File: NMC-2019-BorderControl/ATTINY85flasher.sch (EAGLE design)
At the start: 13 parts, among them J1 ICSP-LO-SILK

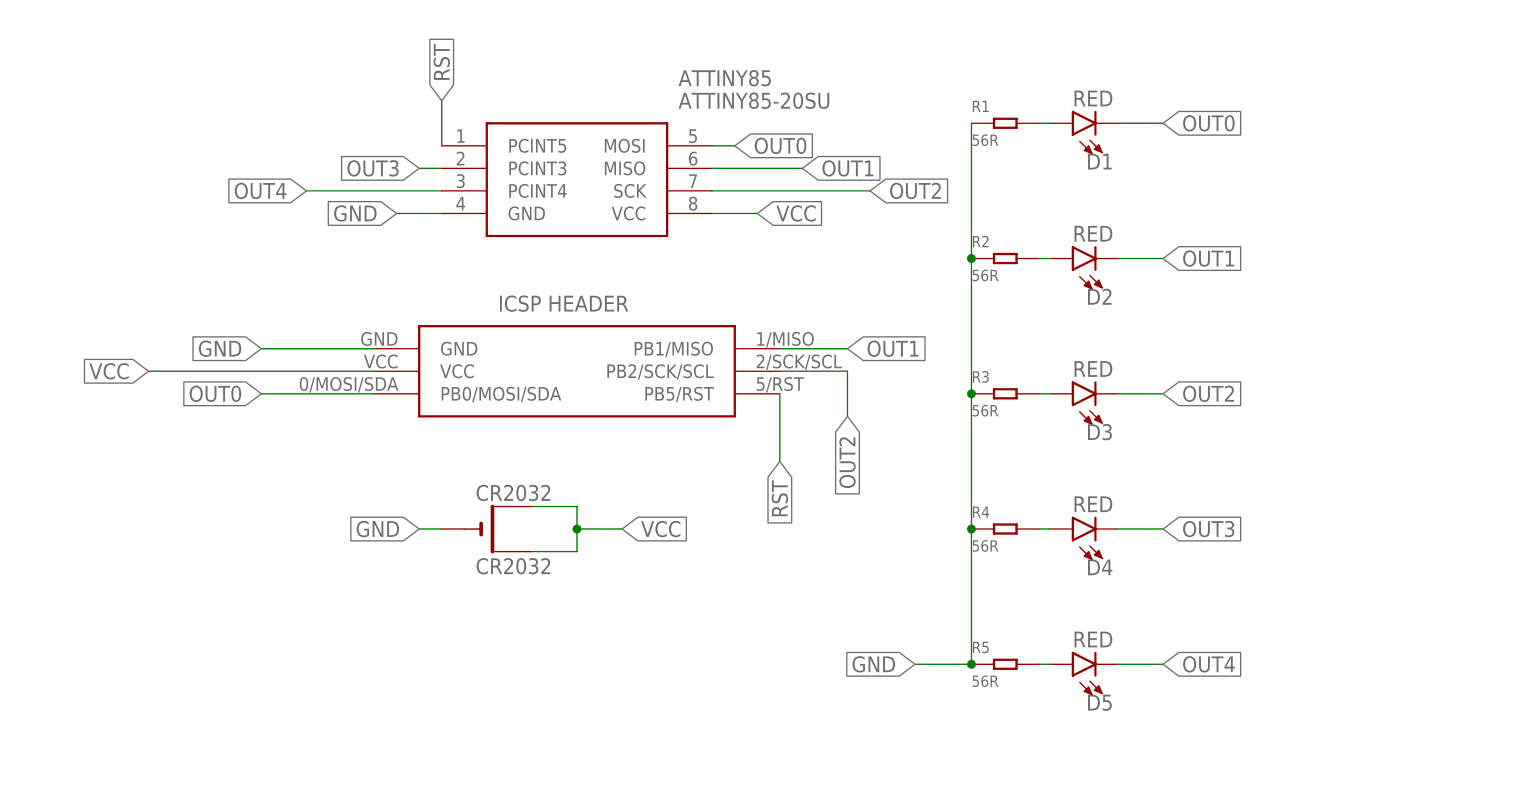
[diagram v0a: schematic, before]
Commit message: corrected polarity
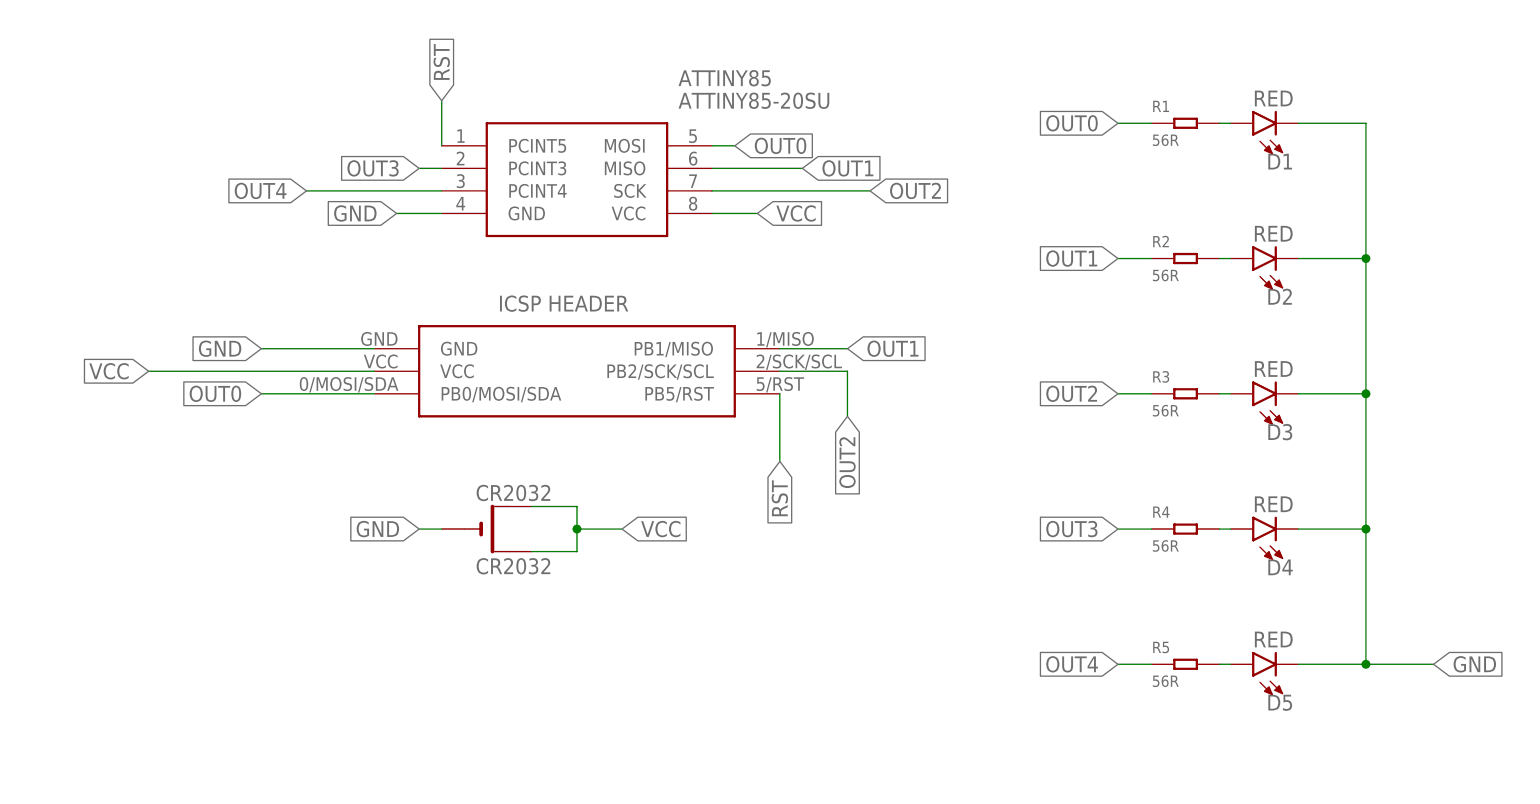
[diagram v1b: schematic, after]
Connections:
- net GND: now also D1.C, D2.C, D3.C, D4.C, D5.C; no longer R1.1, R2.1, R3.1, R4.1, R5.1
- net OUT0: now also R1.1; no longer D1.C
- net OUT1: now also R2.1; no longer D2.C
- net OUT2: now also R3.1; no longer D3.C
- net OUT3: now also R4.1; no longer D4.C
- net OUT4: now also R5.1; no longer D5.C
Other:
- moved on the sheet: D1, D2, D3, D4, D5, R1, R2, R3, R4, R5

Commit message: added decoupling cap to pcb
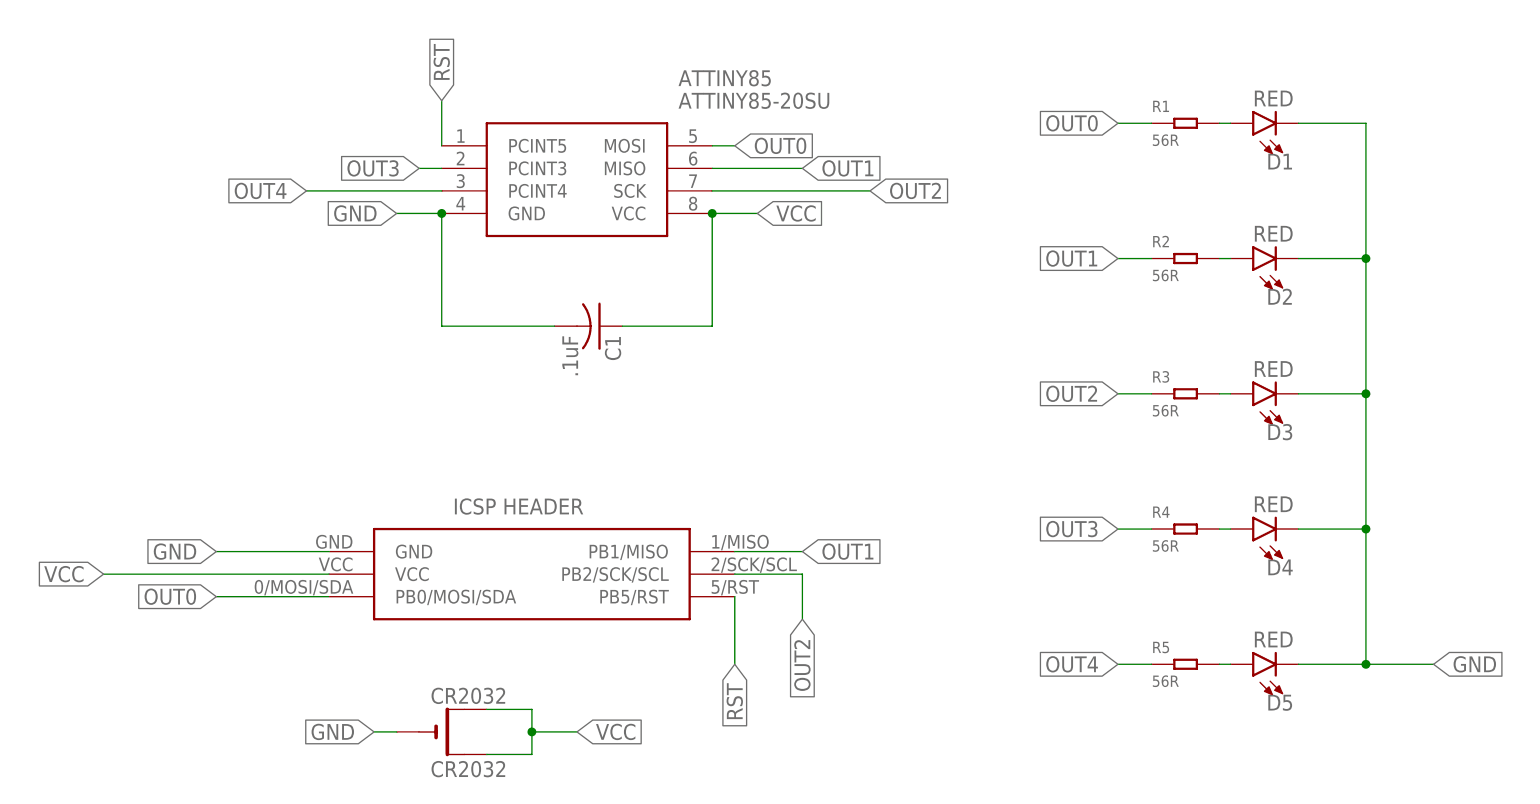
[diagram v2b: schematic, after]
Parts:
- added C1: .1uF, adafruit:C-USC0603
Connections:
- net GND: now also C1.2
- net VCC: now also C1.1
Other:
- moved on the sheet: CR2032
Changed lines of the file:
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@@
 <part name="R5" library="Seeed-Resistor" deviceset="SMD-RES-13R-5%-1/4W(1206)" device="" value="56R"/>
 <part name="J1" library="BadgeParts" deviceset="ICSP-LO-SILK" device=""/>
+<part name="C1" library="adafruit" library_urn="urn:adsk.eagle:library:420" deviceset="C-US" device="C0603" package3d_urn="urn:adsk.eagle:package:6240338/1" value=".1uF"/>
 </parts>
 <sheets>
@@
 </plain>
 <instances>
-<instance part="CR2032" gate="G$1" x="25.4" y="35.56" smashed="yes">
-<attribute name="NAME" x="24.13" y="38.735" size="1.778" layer="95"/>
-<attribute name="VALUE" x="24.13" y="30.48" size="1.778" layer="96"/>
+<instance part="CR2032" gate="G$1" x="20.32" y="12.7" smashed="yes">
+<attribute name="NAME" x="19.05" y="15.875" size="1.778" layer="95"/>
+<attribute name="VALUE" x="19.05" y="7.62" size="1.778" layer="96"/>
 </instance>
 <instance part="ATTINY85" gate="G$1" x="20.32" y="78.74" smashed="yes">
@@
 <attribute name="VALUE" x="100.33" y="17.78" size="1.27" layer="96" ratio="10"/>
 </instance>
-<instance part="J1" gate="G$1" x="25.4" y="53.34" smashed="yes"/>
+<instance part="J1" gate="G$1" x="20.32" y="30.48" smashed="yes"/>
+<instance part="C1" gate="G$1" x="38.1" y="58.42" smashed="yes" rot="R270">
+<attribute name="NAME" x="38.735" y="57.404" size="1.778" layer="95" rot="R270"/>
+<attribute name="VALUE" x="33.909" y="57.404" size="1.778" layer="96" rot="R270"/>
+</instance>
 </instances>
 <busses>
@@
 <wire x1="50.8" y1="71.12" x2="55.88" y2="71.12" width="0.1524" layer="91"/>
 <label x="55.88" y="71.12" size="1.778" layer="95" xref="yes"/>
+<pinref part="C1" gate="G$1" pin="1"/>
+<wire x1="40.64" y1="58.42" x2="50.8" y2="58.42" width="0.1524" layer="91"/>
+<wire x1="50.8" y1="58.42" x2="50.8" y2="71.12" width="0.1524" layer="91"/>
+<junction x="50.8" y="71.12"/>
 </segment>
 <segment>
 <pinref part="CR2032" gate="G$1" pin="+"/>
-<wire x1="30.48" y1="38.1" x2="35.56" y2="38.1" width="0.1524" layer="91"/>
-<wire x1="35.56" y1="38.1" x2="35.56" y2="35.56" width="0.1524" layer="91"/>
+<wire x1="25.4" y1="15.24" x2="30.48" y2="15.24" width="0.1524" layer="91"/>
+<wire x1="30.48" y1="15.24" x2="30.48" y2="12.7" width="0.1524" layer="91"/>
 <pinref part="CR2032" gate="G$1" pin="+1"/>
-<wire x1="35.56" y1="35.56" x2="35.56" y2="33.02" width="0.1524" layer="91"/>
-<wire x1="35.56" y1="33.02" x2="30.48" y2="33.02" width="0.1524" layer="91"/>
-<junction x="35.56" y="35.56"/>
-<wire x1="35.56" y1="35.56" x2="40.64" y2="35.56" width="0.1524" layer="91"/>
-<label x="40.64" y="35.56" size="1.778" layer="95" xref="yes"/>
+<wire x1="30.48" y1="12.7" x2="30.48" y2="10.16" width="0.1524" layer="91"/>
+<wire x1="30.48" y1="10.16" x2="25.4" y2="10.16" width="0.1524" layer="91"/>
+<junction x="30.48" y="12.7"/>
+<wire x1="30.48" y1="12.7" x2="35.56" y2="12.7" width="0.1524" layer="91"/>
+<label x="35.56" y="12.7" size="1.778" layer="95" xref="yes"/>
 </segment>
 <segment>
 <pinref part="J1" gate="G$1" pin="VCC"/>
-<wire x1="12.7" y1="53.34" x2="-12.7" y2="53.34" width="0.1524" layer="91"/>
-<label x="-12.7" y="53.34" size="1.778" layer="95" rot="R180" xref="yes"/>
+<wire x1="7.62" y1="30.48" x2="-17.78" y2="30.48" width="0.1524" layer="91"/>
+<label x="-17.78" y="30.48" size="1.778" layer="95" rot="R180" xref="yes"/>
 </segment>
 </net>
@@
 <segment>
 <pinref part="CR2032" gate="G$1" pin="-"/>
-<wire x1="20.32" y1="35.56" x2="17.78" y2="35.56" width="0.1524" layer="91"/>
-<label x="17.78" y="35.56" size="1.778" layer="95" rot="R180" xref="yes"/>
+<wire x1="15.24" y1="12.7" x2="12.7" y2="12.7" width="0.1524" layer="91"/>
+<label x="12.7" y="12.7" size="1.778" layer="95" rot="R180" xref="yes"/>
 </segment>
 <segment>
@@
 <wire x1="20.32" y1="71.12" x2="15.24" y2="71.12" width="0.1524" layer="91"/>
 <label x="15.24" y="71.12" size="1.778" layer="95" rot="R180" xref="yes"/>
+<wire x1="20.32" y1="71.12" x2="20.32" y2="58.42" width="0.1524" layer="91"/>
+<junction x="20.32" y="71.12"/>
+<pinref part="C1" gate="G$1" pin="2"/>
+<wire x1="20.32" y1="58.42" x2="33.02" y2="58.42" width="0.1524" layer="91"/>
 </segment>
 <segment>
 <pinref part="J1" gate="G$1" pin="GND"/>
-<wire x1="12.7" y1="55.88" x2="0" y2="55.88" width="0.1524" layer="91"/>
-<label x="0" y="55.88" size="1.778" layer="95" rot="R180" xref="yes"/>
+<wire x1="7.62" y1="33.02" x2="-5.08" y2="33.02" width="0.1524" layer="91"/>
+<label x="-5.08" y="33.02" size="1.778" layer="95" rot="R180" xref="yes"/>
 </segment>
 <segment>
@@
 <segment>
 <pinref part="J1" gate="G$1" pin="PB0/MOSI/SDA"/>
-<wire x1="12.7" y1="50.8" x2="0" y2="50.8" width="0.1524" layer="91"/>
-<label x="0" y="50.8" size="1.778" layer="95" rot="R180" xref="yes"/>
+<wire x1="7.62" y1="27.94" x2="-5.08" y2="27.94" width="0.1524" layer="91"/>
+<label x="-5.08" y="27.94" size="1.778" layer="95" rot="R180" xref="yes"/>
 </segment>
 <segment>
@@
 <segment>
 <pinref part="J1" gate="G$1" pin="PB1/MISO"/>
-<wire x1="58.42" y1="55.88" x2="66.04" y2="55.88" width="0.1524" layer="91"/>
-<label x="66.04" y="55.88" size="1.778" layer="95" xref="yes"/>
+<wire x1="53.34" y1="33.02" x2="60.96" y2="33.02" width="0.1524" layer="91"/>
+<label x="60.96" y="33.02" size="1.778" layer="95" xref="yes"/>
 </segment>
 <segment>
@@
 <segment>
 <pinref part="J1" gate="G$1" pin="PB2/SCK/SCL"/>
-<wire x1="58.42" y1="53.34" x2="66.04" y2="53.34" width="0.1524" layer="91"/>
-<wire x1="66.04" y1="53.34" x2="66.04" y2="48.26" width="0.1524" layer="91"/>
-<label x="66.04" y="48.26" size="1.778" layer="95" rot="R270" xref="yes"/>
+<wire x1="53.34" y1="30.48" x2="60.96" y2="30.48" width="0.1524" layer="91"/>
+<wire x1="60.96" y1="30.48" x2="60.96" y2="25.4" width="0.1524" layer="91"/>
+<label x="60.96" y="25.4" size="1.778" layer="95" rot="R270" xref="yes"/>
 </segment>
 <segment>
@@
 <segment>
 <pinref part="J1" gate="G$1" pin="PB5/RST"/>
-<wire x1="58.42" y1="50.8" x2="58.42" y2="43.18" width="0.1524" layer="91"/>
-<label x="58.42" y="43.18" size="1.778" layer="95" rot="R270" xref="yes"/>
-</segment>
-</net>
+<wire x1="53.34" y1="27.94" x2="53.34" y2="20.32" width="0.1524" layer="91"/>
+<label x="53.34" y="20.32" size="1.778" layer="95" rot="R270" xref="yes"/>
+</segment>
+</net>

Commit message: added revB firmware and changed battery holder orientation
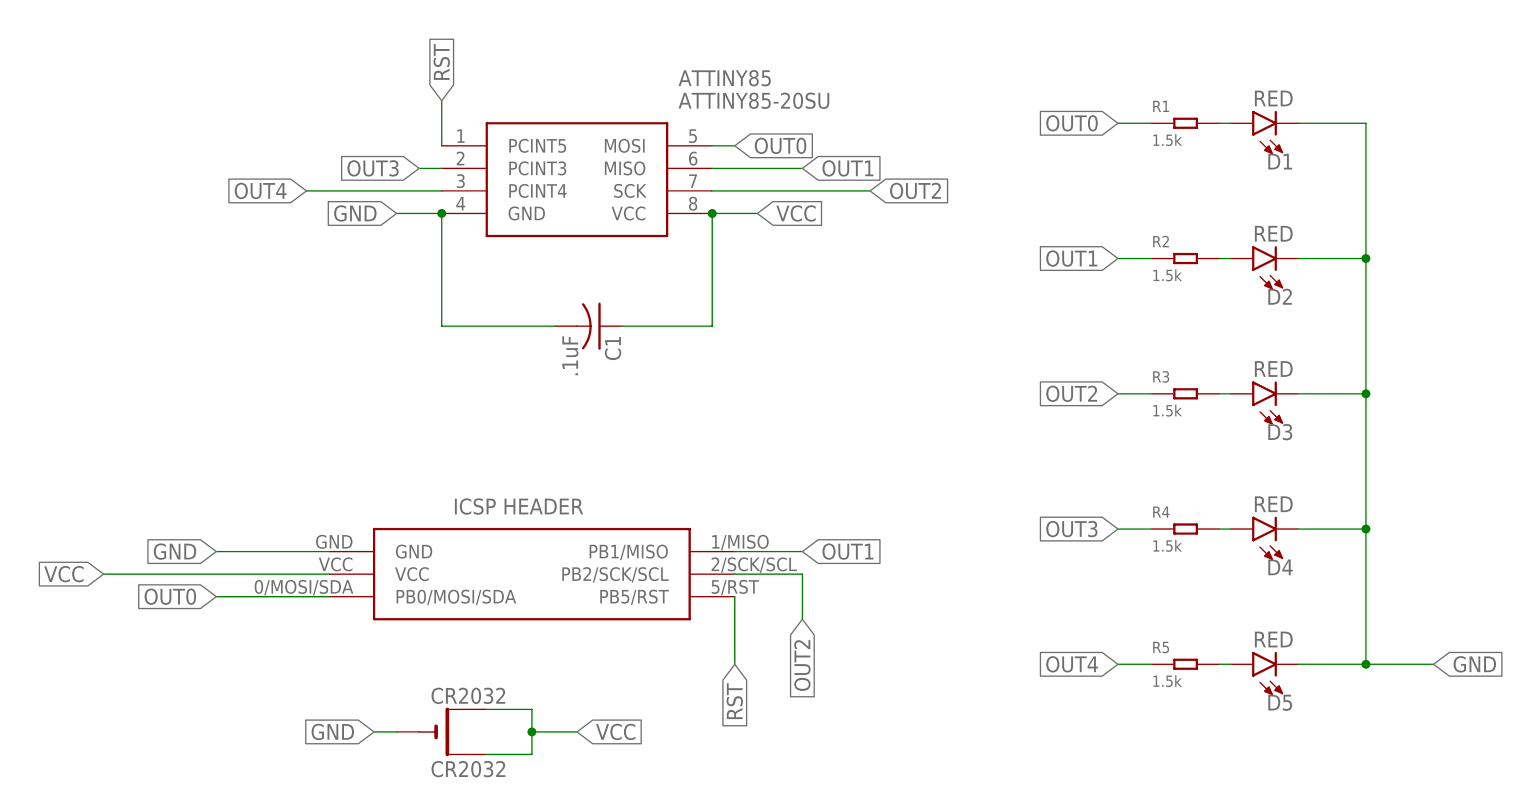
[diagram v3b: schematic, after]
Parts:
- R1, R2, R3, R4, R5: value 56R -> 1.5k
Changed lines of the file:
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@@
 <part name="D4" library="SparkFun-LED" library_urn="urn:adsk.eagle:library:529" deviceset="LED-RED" device="1206" package3d_urn="urn:adsk.eagle:package:39352/1" value="RED"/>
 <part name="D5" library="SparkFun-LED" library_urn="urn:adsk.eagle:library:529" deviceset="LED-RED" device="1206" package3d_urn="urn:adsk.eagle:package:39352/1" value="RED"/>
-<part name="R1" library="Seeed-Resistor" deviceset="SMD-RES-13R-5%-1/4W(1206)" device="" value="56R"/>
-<part name="R2" library="Seeed-Resistor" deviceset="SMD-RES-13R-5%-1/4W(1206)" device="" value="56R"/>
-<part name="R3" library="Seeed-Resistor" deviceset="SMD-RES-13R-5%-1/4W(1206)" device="" value="56R"/>
-<part name="R4" library="Seeed-Resistor" deviceset="SMD-RES-13R-5%-1/4W(1206)" device="" value="56R"/>
-<part name="R5" library="Seeed-Resistor" deviceset="SMD-RES-13R-5%-1/4W(1206)" device="" value="56R"/>
+<part name="R1" library="Seeed-Resistor" deviceset="SMD-RES-13R-5%-1/4W(1206)" device="" value="1.5k"/>
+<part name="R2" library="Seeed-Resistor" deviceset="SMD-RES-13R-5%-1/4W(1206)" device="" value="1.5k"/>
+<part name="R3" library="Seeed-Resistor" deviceset="SMD-RES-13R-5%-1/4W(1206)" device="" value="1.5k"/>
+<part name="R4" library="Seeed-Resistor" deviceset="SMD-RES-13R-5%-1/4W(1206)" device="" value="1.5k"/>
+<part name="R5" library="Seeed-Resistor" deviceset="SMD-RES-13R-5%-1/4W(1206)" device="" value="1.5k"/>
 <part name="J1" library="BadgeParts" deviceset="ICSP-LO-SILK" device=""/>
 <part name="C1" library="adafruit" library_urn="urn:adsk.eagle:library:420" deviceset="C-US" device="C0603" package3d_urn="urn:adsk.eagle:package:6240338/1" value=".1uF"/>
